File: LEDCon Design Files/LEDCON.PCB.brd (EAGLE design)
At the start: 81.7 x 51.7 mm, 24 parts

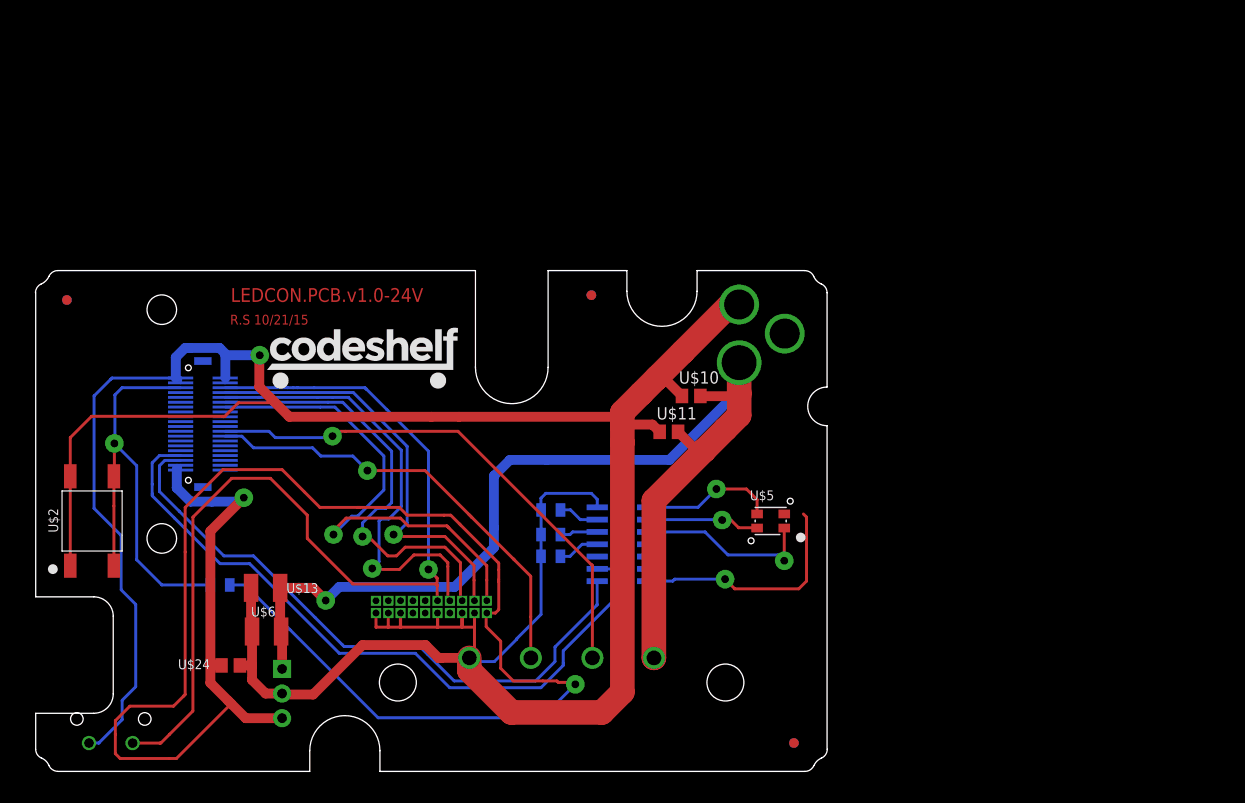
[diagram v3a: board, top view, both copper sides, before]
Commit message: Two-plane isolation version 1
All of the design changes needed to make a 2-plane isolation design.
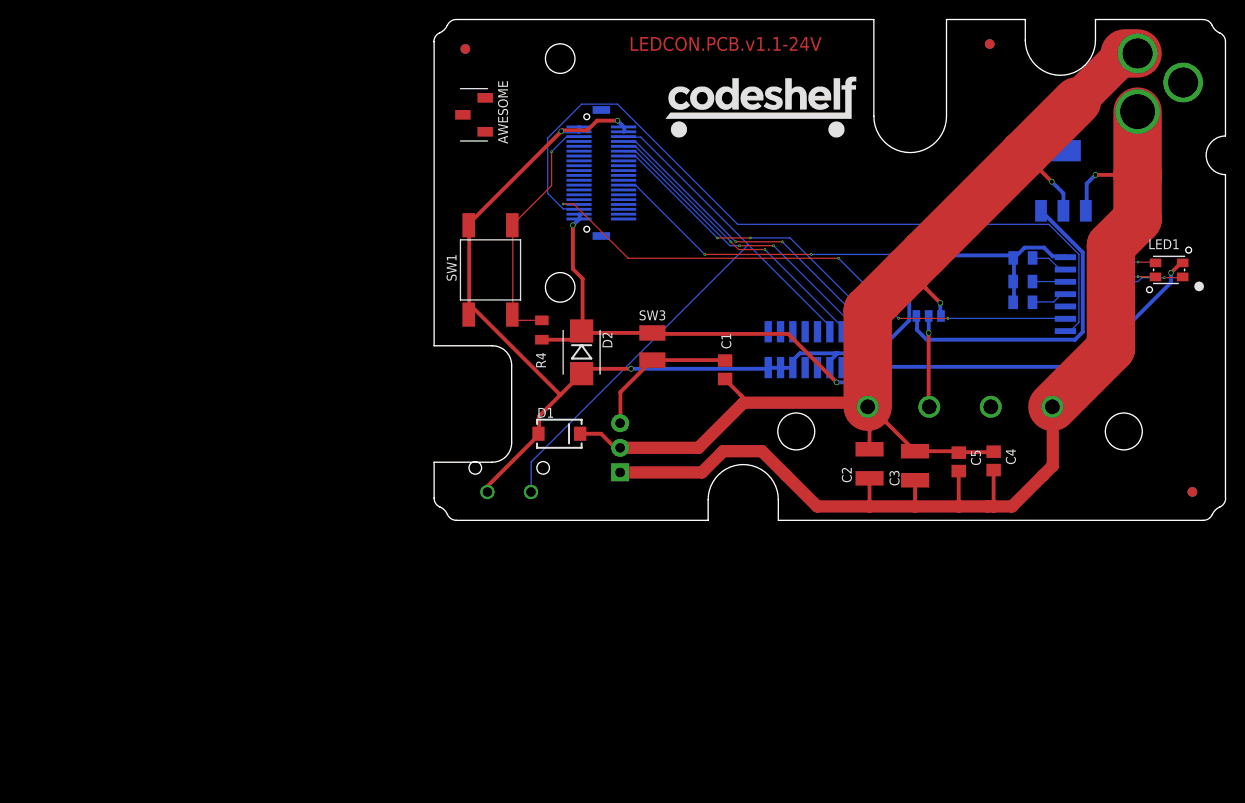
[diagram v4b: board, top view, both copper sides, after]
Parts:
- removed U$1: (no value), KW2:MATE-N-LOK_643230-1
- removed U$10: 0.1uF, GW-devices:C0805
- removed U$11: 1uF, GW-devices:C0805
- removed U$13, U$6: 10uF, GW-devices:C1210K
- removed U$15, U$16, U$17: 24Ohm, GW-devices:RF-C0805
- removed U$19: (no value), KW2:2X10JTAG
- removed U$2: (no value), GW-devices:ESWITCH-TL3301PF
- removed U$24: 10uF, GW-devices:C0805
- removed U$3: (no value), KW2:BARREL_CUI_PJ-002A
- removed U$4: (no value), KW2:DF12_F
- removed U$5: (no value), KW2:PLCC4_SMALL
- removed U$7: 10k, GW-devices:RF-C0805
- removed U$8: (no value), GW-devices:SO14
- removed U$9: (no value), KW2:RA_BUTTON
- added AWESOME: CJS, KW2:CJS
- added C1: 10uF, GW-devices:C0805
- added C2, C3: 10uF, GW-devices:C1210K
- added C4: 1uF, GW-devices:C0805
- added C5: 0.1uF, GW-devices:C0805
- added D1: (no value), SparkFun:SMA-DIODE
- added D2: DIODE-ZENERSMB, SparkFun:SMB-DIODE
- added J1: MATE-N-LOK_643230-1, KW2:MATE-N-LOK_643230-1
- added JTAG: 2X10JTAGSMD, KW2:2X10JTAG-SMD
- added KW2: (no value), KW2:DF12_F
- added LED1: RGLBED, KW2:RGBLED
- added P1: BARREL_CUI_PJ-002A, KW2:BARREL_CUI_PJ-002A
- added R1, R2, R3: 24Ohm, GW-devices:RF-C0805
- added R4: 10k, GW-devices:RF-C0805
- added SW1: SWITCH-TACTILE, GW-devices:ESWITCH-TL3301PF
- added SW2: RA_BUTTON, KW2:RA_BUTTON
- added SW3: SMD050F, GW-devices:C1210
- added U1: WS2801, GW-devices:SO14
- added U2: OPTOCOUPLER, GW-devices:S06-5
- added U3: V_REG_MIC2920, SparkFun:SOT223
- moved U$14 48.6 mm to (78.5, 3.00)
- moved U$18 48.6 mm to (3.50, 48.7)
- moved U$25 48.6 mm to (57.6, 49.2)
- moved U$26 48.6 mm to (57.6, 49.2)
- moved U$27 48.6 mm to (3.50, 48.7)
- moved U$28 48.6 mm to (78.5, 3.00)
- moved IC1 43.1 mm to (19.5, 7.55), turned to 90 degrees
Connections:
- removed net CLK_5V: U$1.P$3, U$4.P$24
- removed net N$3: U$19.P$10, U$4.P$6, U$9.P$1
- new net +5V: U2.P$5, U3.3
- new net GNDA: C1.1, C2.1, C3.1, C4.1, C5.1, D1.C, IC1.GND, J1.P$1, P1.P$2, U2.P$3, U3.2
- new net N$1: C1.2, IC1.OUT, SW3.1
- new net N$2: J1.P$2, U2.P$4
- new net SW2: JTAG.P$10, KW2.P$6, SW2.P$1
- net +3V3: now also D2.C, JTAG.P$1, KW2.P$37, KW2.P$39, LED1.P$2, R4.2, SW3.2, U1.14; no longer IC1.OUT, U$19.P$1, U$24.2, U$4.P$37, U$4.P$39, U$5.P$2, U$7.2, U$8.14
- net DAT_5V: now also KW2.P$26, U2.P$1; no longer U$1.P$2, U$4.P$26
- net GND: now also D1.A, D2.A, JTAG.P$15, JTAG.P$17, JTAG.P$19, JTAG.P$3, JTAG.P$5, JTAG.P$9, KW2.P$1, KW2.P$2, KW2.P$3, KW2.P$4, R1.2, R2.2, R3.2, SW1.1, SW1.2, SW2.P$2, U1.7, U2.P$2; no longer IC1.GND, U$1.P$1, U$10.1, U$11.1, U$13.1, U$15.2, U$16.2, U$17.2, U$19.P$15, U$19.P$17, U$19.P$19, U$19.P$3, U$19.P$5, U$19.P$9, U$2.1, U$2.2, U$24.1, U$3.P$2, U$4.P$1, U$4.P$2, U$4.P$3, U$4.P$4, U$6.1, U$8.7, U$9.P$2
- net N$10: now also KW2.P$33, U1.2; no longer U$4.P$33, U$8.2
- net N$11: now also R1.1, U1.6; no longer U$15.1, U$8.6
- net N$12: now also R2.1, U1.5; no longer U$16.1, U$8.5
- net N$13: now also R3.1, U1.4; no longer U$17.1, U$8.4
- net N$14: now also KW2.P$35, U1.1; no longer U$4.P$35, U$8.1
- net N$18: now also JTAG.P$4, KW2.P$8; no longer U$19.P$4, U$4.P$8
- net N$20: now also JTAG.P$8, KW2.P$10; no longer U$19.P$8, U$4.P$10
- net N$21: now also KW2.P$5, R4.1, SW1.3, SW1.4; no longer U$2.3, U$2.4, U$4.P$5, U$7.1
- net N$4: now also LED1.P$4, U1.9; no longer U$5.P$4, U$8.9
- net N$5: now also LED1.P$3, U1.8; no longer U$5.P$3, U$8.8
- net N$6: now also JTAG.P$2, KW2.P$14; no longer U$19.P$2, U$4.P$14
- net N$7: now also LED1.P$1, U1.10; no longer U$5.P$1, U$8.10
- net N$8: now also JTAG.P$6, KW2.P$12; no longer U$19.P$6, U$4.P$12
- net V+: now also C2.2, C3.2, C4.2, C5.2, J1.P$4, P1.P$1, U3.1; no longer U$1.P$4, U$10.2, U$11.2, U$13.2, U$3.P$1, U$6.2
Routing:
- net GND: track 310.5 -> 131.3 mm, vias 1 -> 3
- net GNDA: track 0.00 -> 120.2 mm, vias 0 -> 2
- net +3V3: track 189.1 -> 88.2 mm, vias 2 -> 3
- net N$3: track 100.0 -> 0.00 mm, vias 1 -> 0
- net SW2: track 0.00 -> 64.7 mm
- net CLK_5V: track 53.8 -> 0.00 mm, vias 1 -> 0
- net V+: track 147.4 -> 111.3 mm, vias 2 -> 1
- net +5V: track 0.00 -> 33.6 mm
- net N$21: track 46.7 -> 25.4 mm
- net N$6: track 51.5 -> 34.1 mm, vias 1 -> 2
- net N$20: track 47.2 -> 30.8 mm, vias 1 -> 2
- net N$14: track 64.9 -> 81.1 mm
- net N$1: track 0.00 -> 15.5 mm
- net N$8: track 45.8 -> 31.8 mm, vias 1 -> 2
- net N$10: track 72.3 -> 58.4 mm, vias 0 -> 4
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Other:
- board text added: "LEDCON.PCB.v1.1-24V"
- board text removed: "LEDCON.PCB.v1.0-24V"
- board text removed: "R.S 10/21/15"

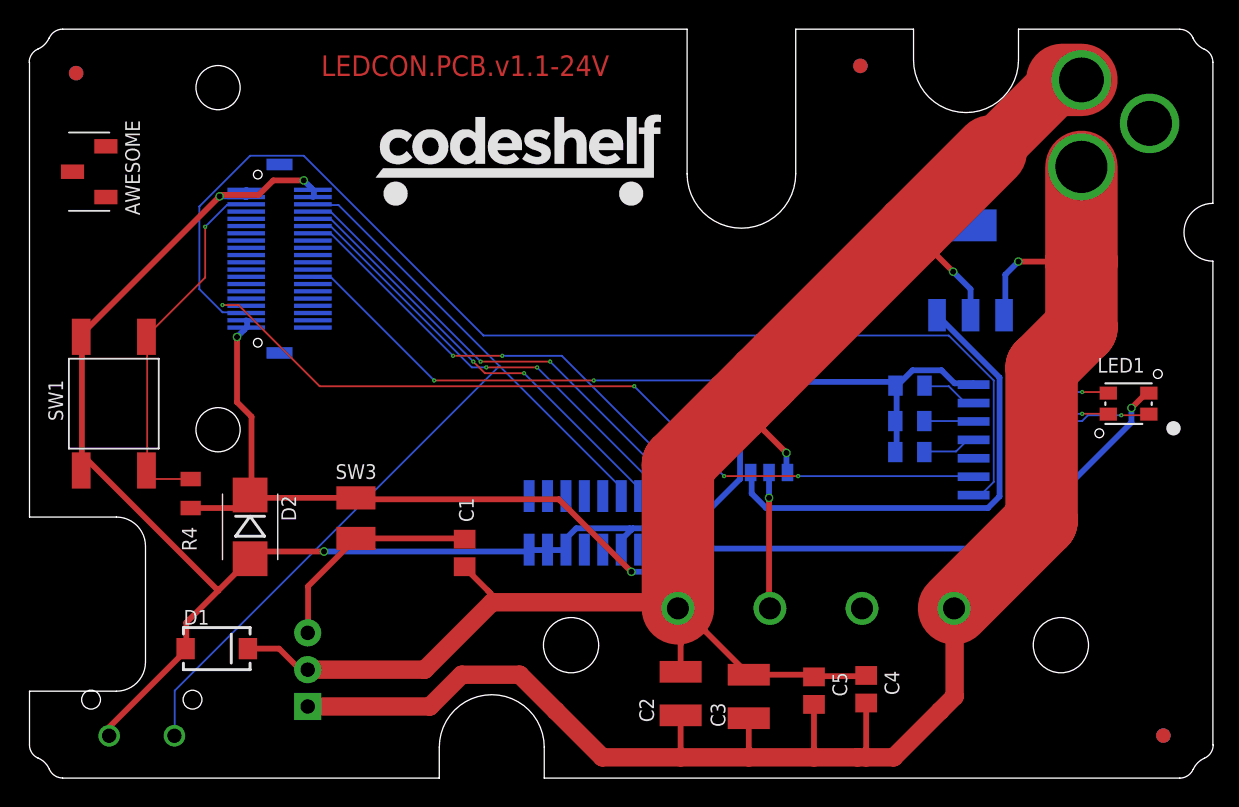
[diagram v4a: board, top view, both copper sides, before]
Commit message: Redo the layout per the Codeshelf.standard DRU file
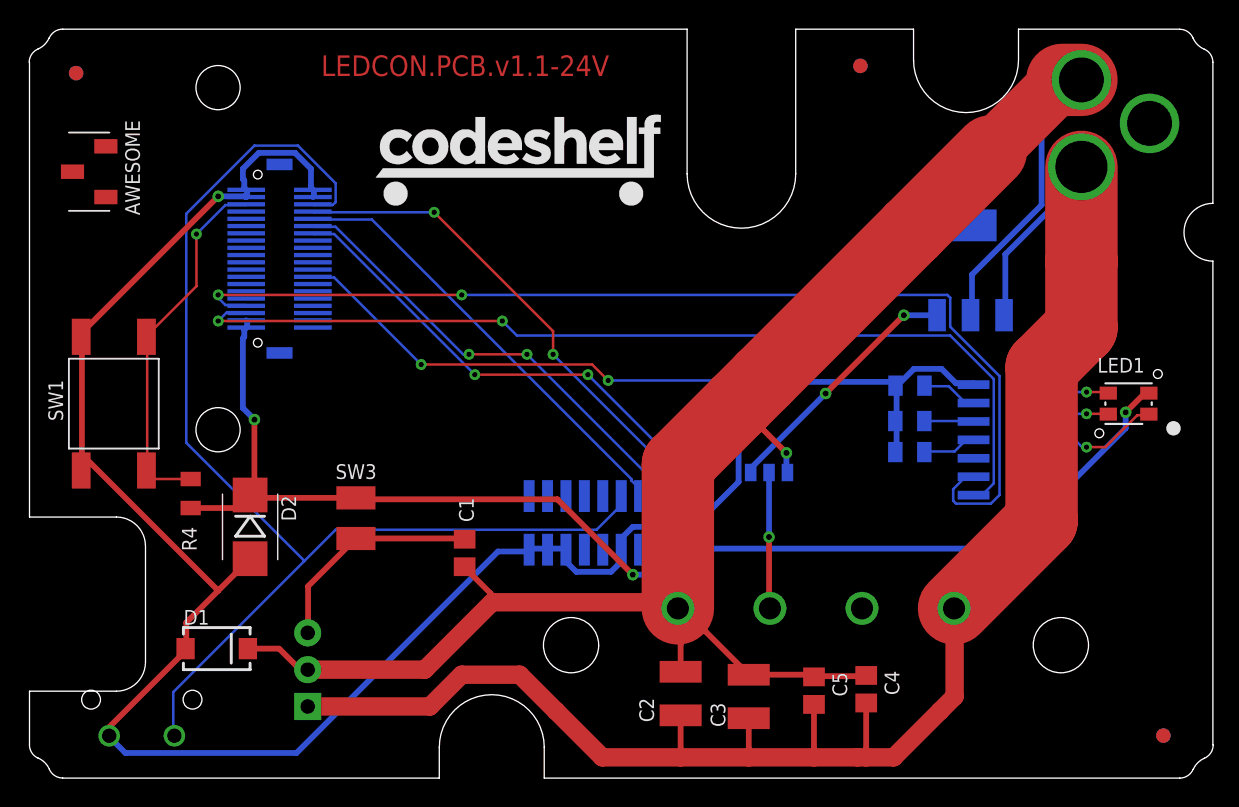
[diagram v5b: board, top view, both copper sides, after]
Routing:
- net SW2: track 64.7 -> 83.6 mm
- net GND: track 131.3 -> 149.7 mm, vias 3 -> 1
- net +5V: track 33.6 -> 17.5 mm, vias 0 -> 2
- net N$10: track 58.4 -> 74.1 mm, vias 4 -> 2
- net N$14: track 81.1 -> 66.3 mm, vias 0 -> 2
- net GNDA: track 120.2 -> 132.2 mm, vias 2 -> 1
- net V+: track 111.3 -> 115.4 mm, vias 1 -> 0
- net N$18: track 33.5 -> 35.5 mm
- net N$7: track 7.14 -> 8.60 mm
- net +3V3: track 88.2 -> 89.2 mm
- net N$6: track 34.1 -> 35.0 mm
- net N$8: track 31.8 -> 32.5 mm
- net N$20: track 30.8 -> 31.4 mm, vias 2 -> 0
